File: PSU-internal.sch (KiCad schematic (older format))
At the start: 35 parts, among them Q3 BD241A

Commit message: Simplified external PSU, now that I've decided to put it in its own case.
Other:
- note removed: "Change TF. Need something that gives >= 7.6 VRMS out.\nTotal VA >= 3.8 W\nhttp://australia.rs-online.com/web/p/pcb-transformers/0504357/\nhttp://au.mouser.com/ProductDetail/TE-Connectivity-PB/4900-9010RC62/?qs=sGAEpiMZZMvwUzoUXIIvybxvWcHlXqMIJJMreLPLlIY%3d\nhttp://au.mouser.com/ProductDetail/Hammond-Manufacturing/160G10/?qs=sGAEpiMZZMvwUzoUXIIvyW8HfC4QLhUeoMmGdCqPnA8%3d"
- note removed: "TF needs to give >= 17 VRMS out of each secondary.\nTotal VA >= 17 W\nhttp://australia.rs-online.com/web/p/pcb-transformers/1739298/\nhttp://australia.rs-online.com/web/p/pcb-transformers/1739361/\nhttp://au.mouser.com/ProductDetail/Triad-Magnetics/FS36-1000/?qs=sGAEpiMZZMvwUzoUXIIvydH8%2fj5UF54ye%252bQIrzt8fZs%3d\nhttp://au.mouser.com/ProductDetail/Triad-Magnetics/FS48-750/?qs=sGAEpiMZZMvwUzoUXI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"
- moved on the sheet: C12, C14, C8, C?, D?, Q3, R11, R12, R15, R9, R?, U?

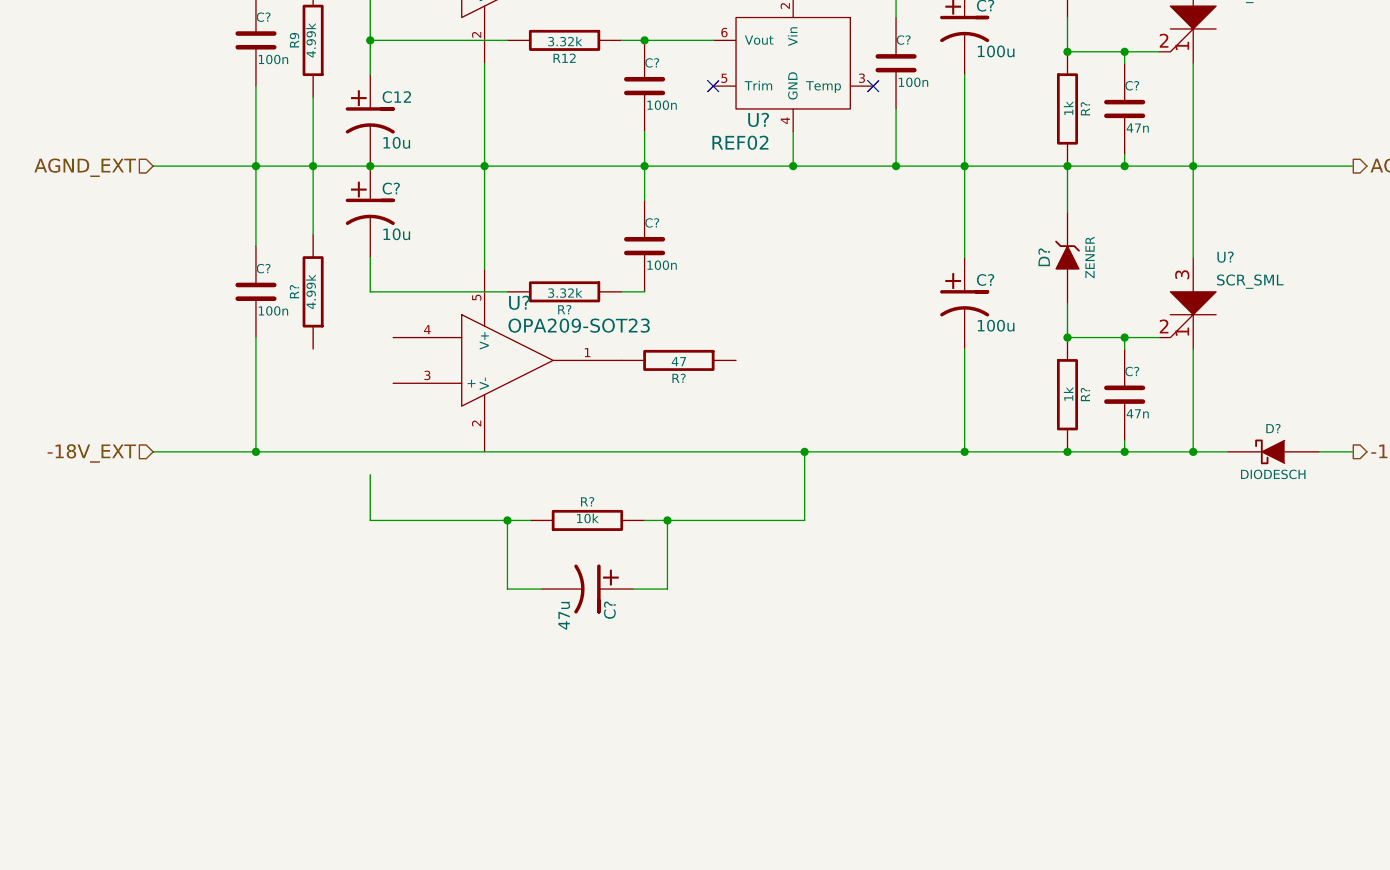
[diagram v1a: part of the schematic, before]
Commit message: Added an analysis of the low pass filter present in the PCM4222EVM differential input stage.
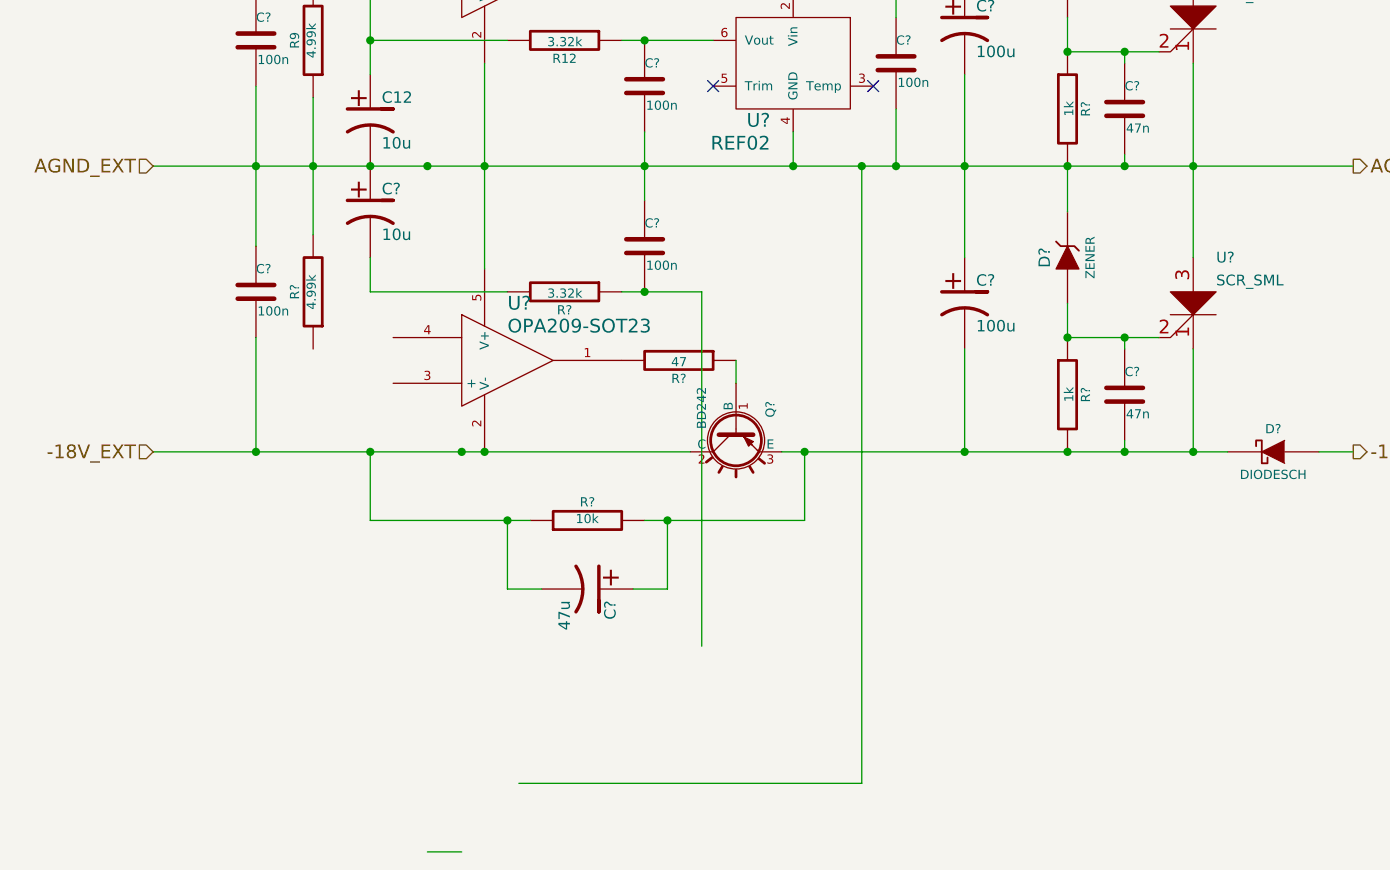
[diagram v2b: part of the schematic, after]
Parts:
- added Q?: BD242, TO220, symbol BD242
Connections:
- wire segments 65 -> 71
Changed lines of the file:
@@
 LIBS:my-conn
 LIBS:ADC-cache
-EELAYER 27 0
+EELAYER 24 0
 EELAYER END
 $Descr A4 11693 8268
@@
 Connection ~ 3200 5750
 Wire Wire Line
-	4900 5050 4800 5050
+	4800 5050 5150 5050
 Wire Wire Line
 	4300 5050 3700 5050
@@
 Connection ~ 5600 5750
 Wire Wire Line
-	4400 6050 3700 6050
-Wire Wire Line
-	3700 6050 3700 5850
+	3700 6050 4400 6050
+Wire Wire Line
+	3700 5750 3700 6050
 Wire Wire Line
 	4450 6350 4300 6350
@@
 Wire Wire Line
 	2750 3250 5100 3250
-Wire Wire Line
-	2750 5750 7450 5750
 Text HLabel 2750 3250 0    60   Input ~ 0
 +18V_EXT
@@
 Text HLabel 2750 5750 0    60   Input ~ 0
 -18V_EXT
+$Comp
+L BD242 Q?
+U 1 1 536B497F
+P 5300 5650
+F 0 "Q?" H 5250 5500 40  0000 R CNN
+F 1 "BD242" H 5300 5800 40  0000 R CNN
+F 2 "TO220" H 5180 5755 29  0001 C CNN
+F 3 "" H 5300 5650 60  0000 C CNN
+	1    5300 5650
+	0    -1   1    0
+$EndComp
+Wire Wire Line
+	5300 5350 5300 5450
+Wire Wire Line
+	2750 5750 5100 5750
+Connection ~ 3700 5750
+Connection ~ 4200 5750
+Wire Wire Line
+	7450 5750 5500 5750
+Connection ~ 3950 4500
+Wire Wire Line
+	3950 7500 4100 7500
+Connection ~ 4100 5750
+Wire Wire Line
+	5150 6600 5150 5050
+Connection ~ 4900 5050
+Wire Wire Line
+	4350 7200 5850 7200
+Wire Wire Line
+	5850 7200 5850 4500
+Connection ~ 5850 4500
 $EndSCHEMATC

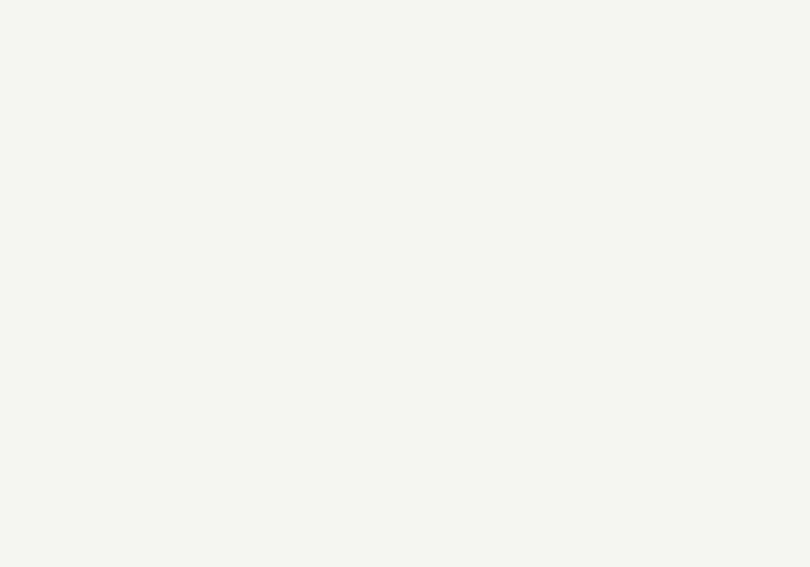
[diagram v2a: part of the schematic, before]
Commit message: Completed the overall system layout, added clipping and input stages.
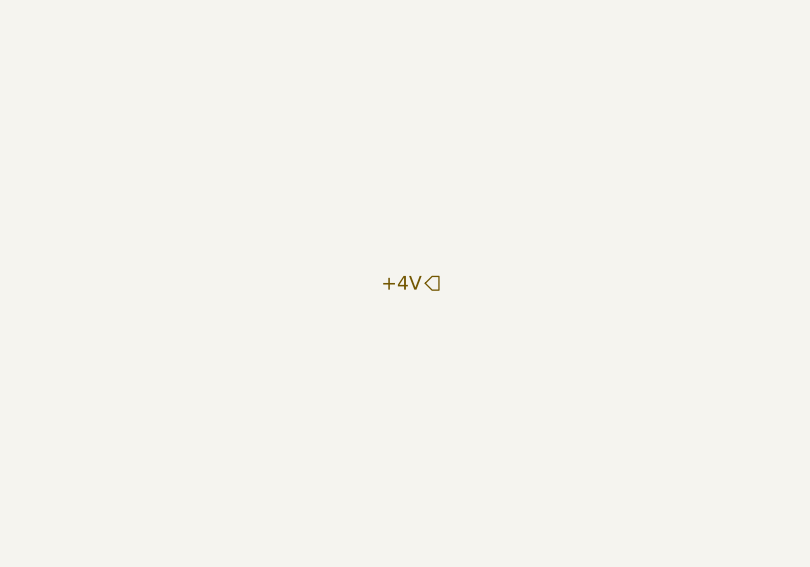
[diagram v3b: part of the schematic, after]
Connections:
- net labels added: +4V
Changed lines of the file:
@@
 LIBS:my-conn
 LIBS:ADC-cache
-EELAYER 24 0
+EELAYER 27 0
 EELAYER END
 $Descr A4 11693 8268
 encoding utf-8
-Sheet 3 5
+Sheet 2 6
 Title ""
-Date "7 may 2014"
+Date "10 may 2014"
 Rev ""
 Comp ""
@@
 	5850 7200 5850 4500
 Connection ~ 5850 4500
+Text HLabel 10400 2450 0    60   Output ~ 0
++4V
 $EndSCHEMATC

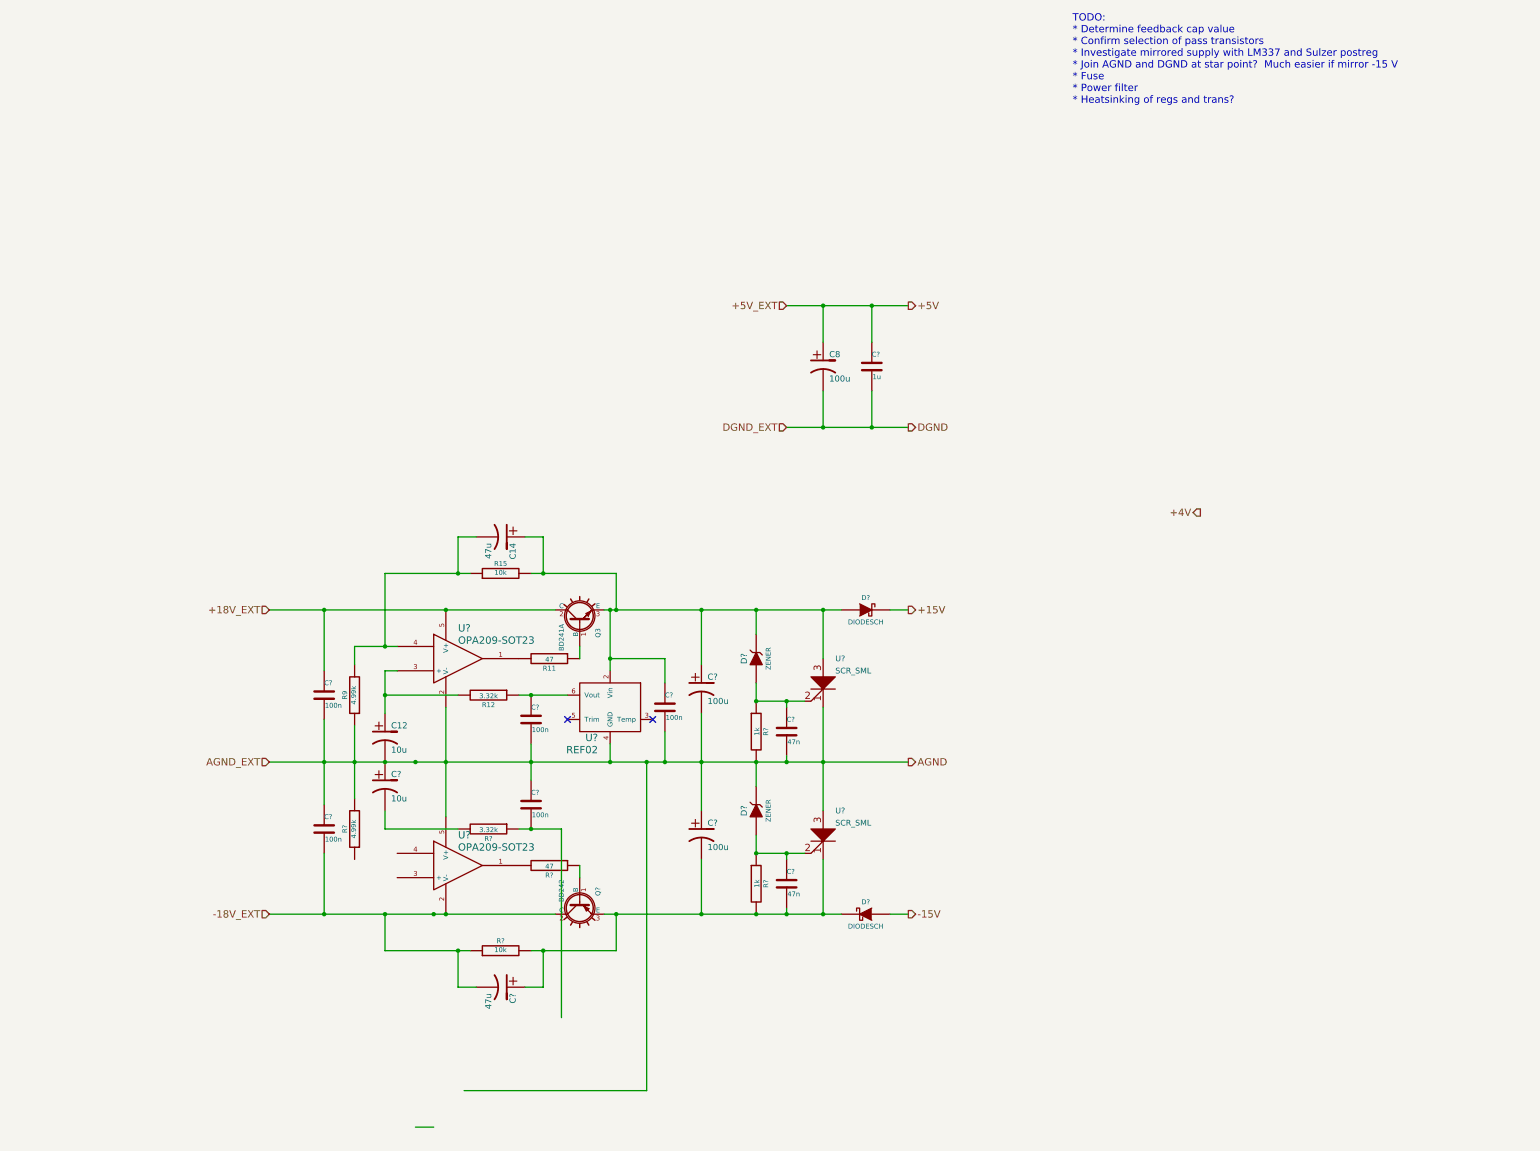
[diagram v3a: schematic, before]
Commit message: Expanded the internal PSU to include a 4 V supply.  Started on reference sharing.
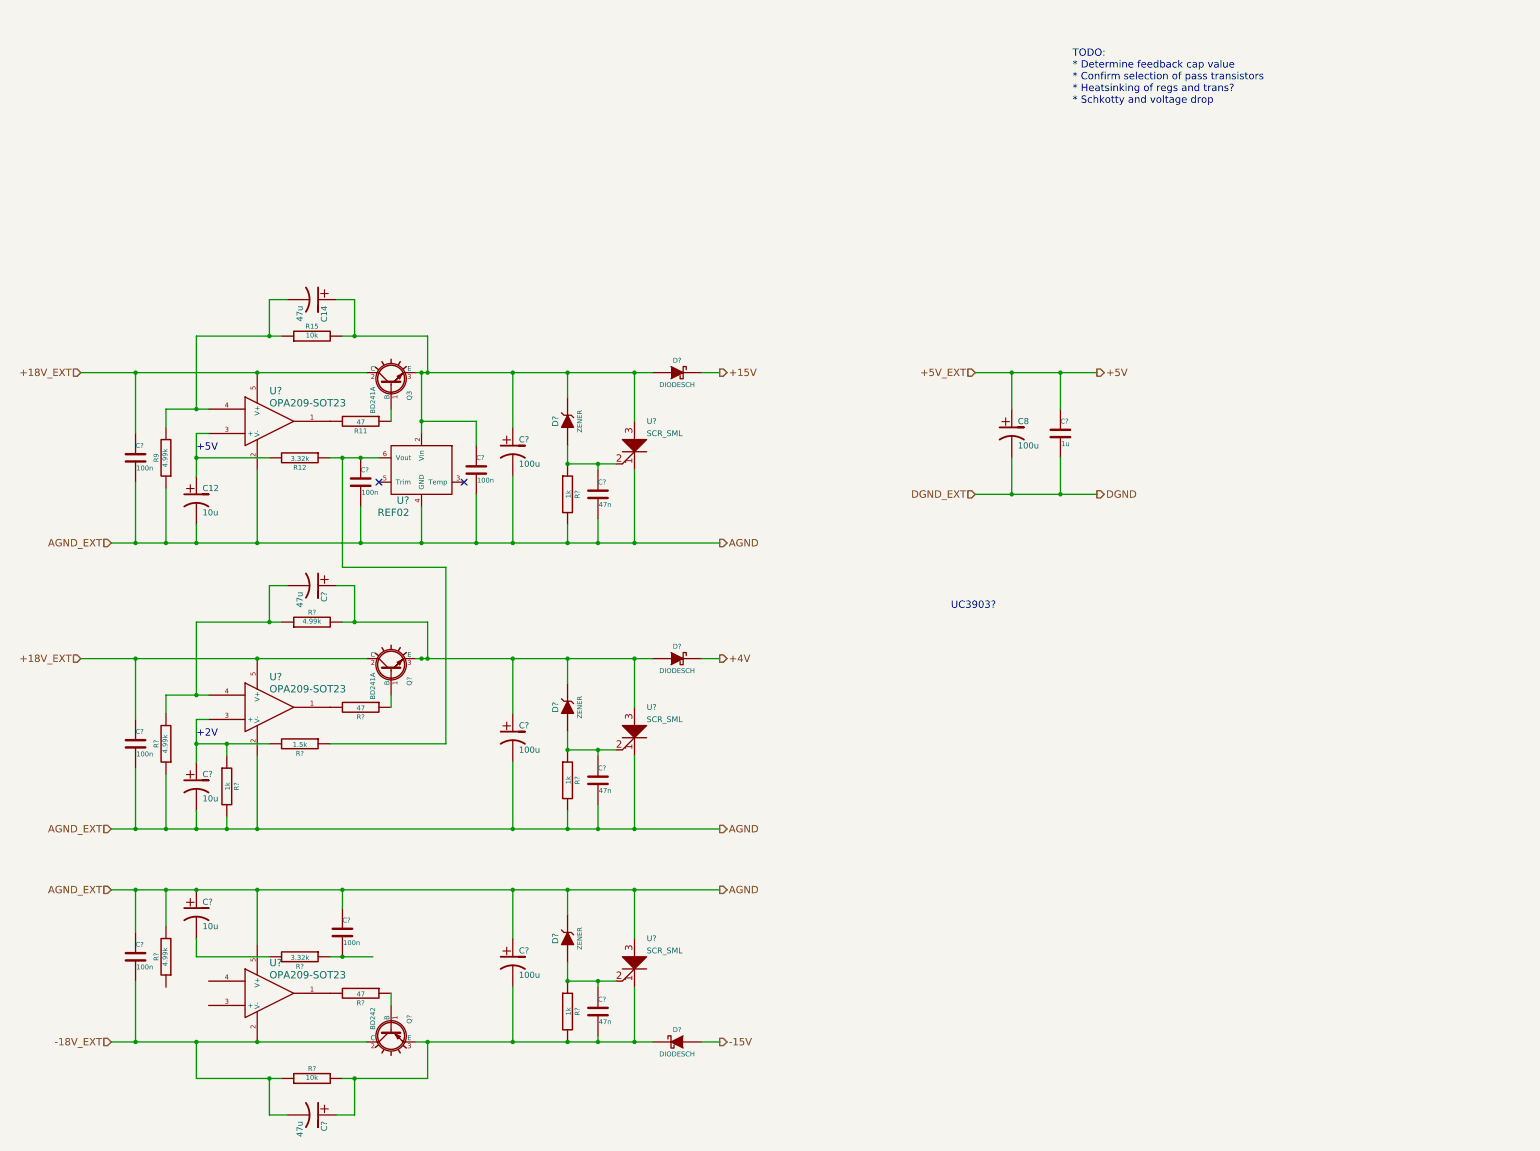
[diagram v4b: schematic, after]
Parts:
- added C?: 47u, symbol CP1
- added C?: 10u, symbol CP1
- added C?: 100u, symbol CP1
- added C?: 100n, symbol C
- added C?: 47n, symbol C
- added D?: ZENER, symbol ZENER
- added D?: DIODESCH, symbol DIODESCH
- added Q?: BD241A, TO-220, symbol BD241A
- added R?: 1k, ~, symbol R
- added R?: 47, symbol R
- added R? (x2): 4.99k, ~, symbol R
- added R?: 1.5k, ~, symbol R
- added R?: 1k, symbol R
- added U?: OPA209-SOT23, symbol OPA209-SOT23
- added U?: SCR_SML, symbol SCR_SML
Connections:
- wire segments 71 -> 115
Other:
- note added: "+2V"
- note added: "+5V"
- note added: "TODO:\n* Determine feedback cap value\n* Confirm selection of pass transistors\n* Heatsinking of regs and trans?\n* Schkotty and voltage drop"
- note added: "UC3903?"
- note removed: "TODO:\n* Determine feedback cap value\n* Confirm selection of pass transistors\n* Investigate mirrored supply with LM337 and Sulzer postreg\n* Join AGND and DGND at star point? Much easier if mirror -15 V\n* Fuse\n* Power filter\n* Heatsinking of regs and trans?"
- moved on the sheet: C12, C14, C8, C?, D?, Q3, Q?, R11, R12, R15, R9, R?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
